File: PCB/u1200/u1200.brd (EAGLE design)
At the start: 243.8 x 243.8 mm, 120 parts, among them IC1 74LS74D, J1 ATX24RH, P1 CBM_A1200_EDGE_CONNECTOR, U16 DRAM_256KX16, U17 DRAM_256KX16, U18 DRAM_256KX16, U19 DRAM_256KX16, U2 CBM_8374, U20 CBM_391425, U4 CBM_4203, U6A AM29F400S, U6B AM29F400S

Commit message: A and DRA bus manual routing
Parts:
- removed R151A, R151B, R151C, R151D, R151E, R151F, R151G, R151H: 68, rcl:R0805
- added R151AH: 742C043680JP, Resistor Array:742C163220JP
- R151I: device rcl:R0805 -> rcl:R0603
- moved ROM_SW 192.8 mm to (226.1, 118.1)
- moved U20 175.8 mm to (205.7, 0.00)
- moved E131C 91.5 mm to (139.7, 63.5)
- moved E131R 91.5 mm to (139.7, 61.0)
- moved R100 91.5 mm to (139.7, 58.4)
- moved R592 82.4 mm to (131.8, 9.91)
- moved R953A 82.4 mm to (131.8, 5.33)
- moved R953B 82.4 mm to (131.8, 7.62)
- moved R953C 82.4 mm to (131.8, 30.5)
- moved R953D 82.4 mm to (131.8, 28.2)
- moved R953E 82.4 mm to (131.8, 25.9)
- moved R953F 82.4 mm to (131.8, 23.6)
- moved R954A 82.4 mm to (131.8, 21.3)
- moved R954B 82.4 mm to (131.8, 19.1)
- moved R954C 82.4 mm to (131.8, 16.8)
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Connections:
- net A17: now also U6A.3; no longer U6A.34
- net A18: now also U6A.34
- net A19: no longer U6A.3
- net BDRA0: now also R151AH.16; no longer R151A.2
- net BDRA1: now also R151AH.15; no longer R151B.2
- net BDRA2: now also R151AH.14; no longer R151C.2
- net BDRA3: now also R151AH.13; no longer R151D.2
- net BDRA4: now also R151AH.12; no longer R151E.2
- net BDRA5: now also R151AH.11; no longer R151F.2
- net BDRA6: now also R151AH.10; no longer R151G.2
- net BDRA7: now also R151AH.9; no longer R151H.2
- net DRA0: now also R151AH.1; no longer R151A.1
- net DRA1: now also R151AH.2; no longer R151B.1
- net DRA2: now also R151AH.3; no longer R151C.1
- net DRA3: now also R151AH.4; no longer R151D.1
- net DRA4: now also R151AH.5; no longer R151E.1
- net DRA5: now also R151AH.6; no longer R151F.1
- net DRA6: now also R151AH.7; no longer R151G.1
- net DRA7: now also R151AH.8; no longer R151H.1
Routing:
- net A10: track 0.00 -> 139.1 mm
- net A19: track 0.00 -> 87.5 mm
- net DRD0: track 0.00 -> 73.1 mm
- net A11: track 0.00 -> 61.3 mm
- net A8: track 0.00 -> 61.2 mm
- net A9: track 0.00 -> 61.1 mm
- net _BRAS_UU: track 0.00 -> 60.3 mm, vias 0 -> 1
- net _BRAS_UM: track 0.00 -> 59.9 mm, vias 0 -> 1
- net DRD18: track 0.00 -> 52.7 mm, vias 0 -> 1
- net DRD17: track 0.00 -> 52.6 mm, vias 0 -> 1
- net DRD16: track 0.00 -> 52.2 mm, vias 0 -> 1
- net A7: track 0.00 -> 47.4 mm
- net A12: track 0.00 -> 46.8 mm
- net A13: track 0.00 -> 45.9 mm
- net A15: track 0.00 -> 44.9 mm
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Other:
- board text removed: "CBM 391425 "BUDGIE""
- board text removed: "CBM 8374 "ALICE""
- board text removed: "Kickstart - High Word"
- board text removed: "Kickstart - Low Word"
- board text removed: "U2"
- board text removed: "U20"

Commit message: a0-a20 bus from edge connector to chip ram
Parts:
- moved X1 229.3 mm to (231.1, 132.1)
- moved U20 177.9 mm to (67.3, 111.8)
- moved U6B 33.0 mm to (57.1, 77.5), turned to 0 degrees
- moved U6A 16.3 mm to (57.1, 55.9), turned to 0 degrees
- moved C902 11.5 mm to (9.65, 25.4)
- moved C901 10.2 mm to (10.2, 27.9)
- moved R593 8.77 mm to (28.3, 26.0), turned to 180 degrees
- moved IC1 7.62 mm to (20.3, 29.2), turned to 0 degrees
- moved R902 6.35 mm to (5.46, 30.5)
- moved R901 5.08 mm to (5.46, 27.9)
- moved R903 3.81 mm to (5.46, 25.4)
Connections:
- net A17: no longer U6A.3
- net A19: now also U6A.3
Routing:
- net A20: track 0.00 -> 166.0 mm, vias 0 -> 2
- net A1: track 0.00 -> 135.6 mm
- net A0: track 0.00 -> 95.6 mm
- net A18: track 44.2 -> 129.4 mm, vias 0 -> 2
- net A17: track 41.2 -> 124.3 mm, vias 0 -> 1
- net A16: track 44.3 -> 122.0 mm, vias 0 -> 2
- net A15: track 44.9 -> 117.1 mm, vias 0 -> 1
- net A14: track 44.8 -> 116.7 mm, vias 0 -> 2
- net A13: track 45.9 -> 116.4 mm, vias 0 -> 1
- net A12: track 46.8 -> 111.5 mm, vias 0 -> 2
- net A5: track 44.5 -> 103.3 mm, vias 0 -> 1
- net A4: track 44.6 -> 102.2 mm
- net A2: track 41.9 -> 99.2 mm
- net A6: track 44.5 -> 101.8 mm
- net A3: track 43.1 -> 98.7 mm, vias 0 -> 1
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
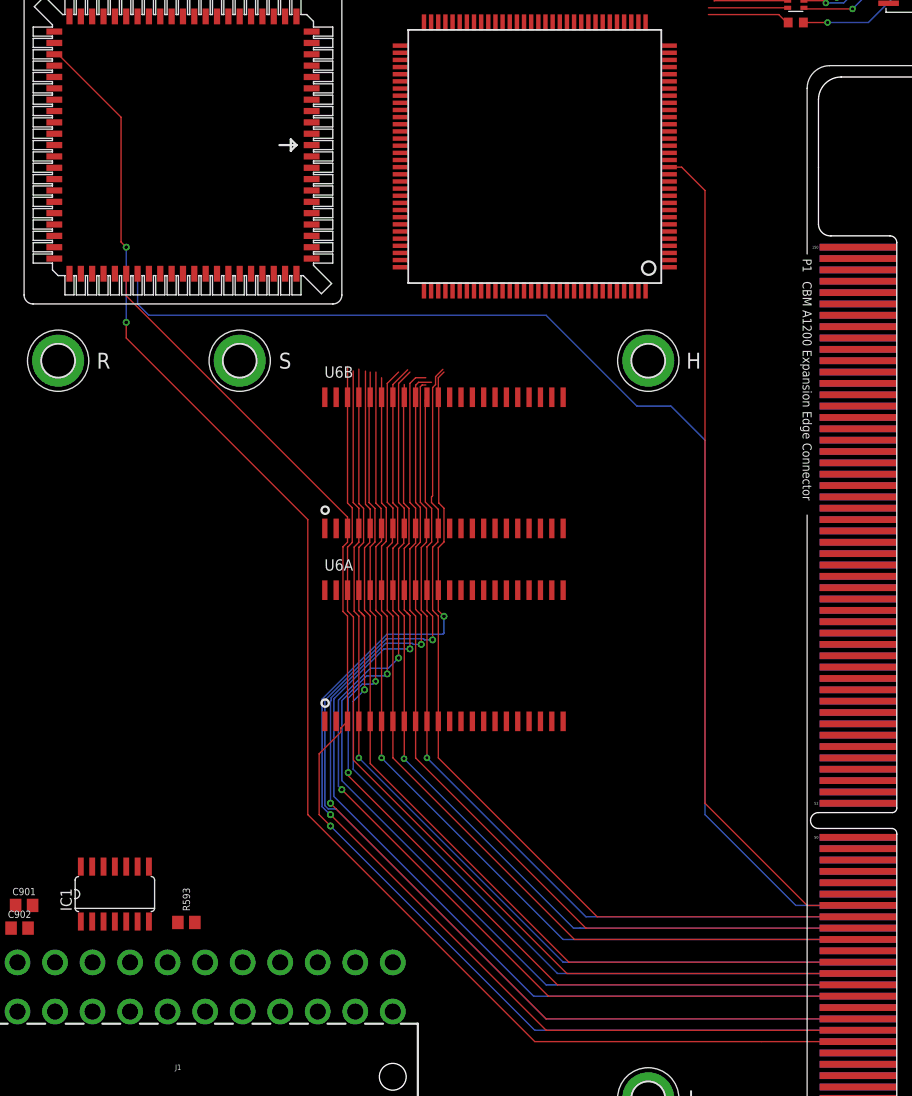
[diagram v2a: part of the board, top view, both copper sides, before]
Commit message: a0-a120 chipram/edge connector bus moved to top layer
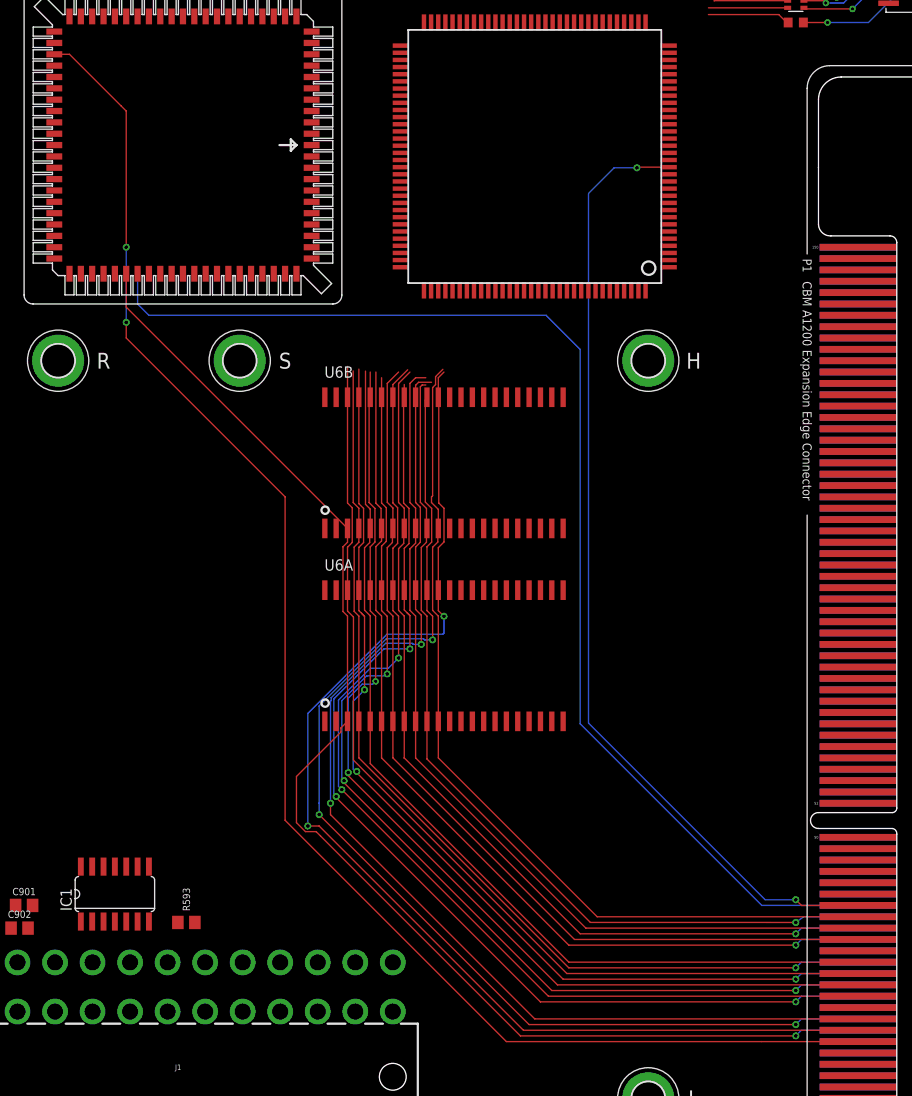
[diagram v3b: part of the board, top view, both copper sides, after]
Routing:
- net A0: track 95.6 -> 108.1 mm, vias 0 -> 2
- net A19: track 139.7 -> 147.5 mm
- net A11: track 109.2 -> 113.0 mm, vias 1 -> 3
- net A15: track 117.1 -> 120.9 mm, vias 1 -> 3
- net A9: track 106.2 -> 109.9 mm
- net A7: track 102.6 -> 106.3 mm
- net A18: track 129.4 -> 132.9 mm
- net A20: track 166.0 -> 168.6 mm
- net A17: track 124.3 -> 126.4 mm, vias 1 -> 3
- net A16: track 122.0 -> 122.7 mm
- net A13: track 116.4 -> 117.0 mm, vias 1 -> 3
- net A3: track 98.7 -> 99.2 mm

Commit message: Added License
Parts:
- removed R951A, R951B, R951C, R951D, R951E, R951F, R951G: 4.7K, rcl:R0805
- added R951AG: 741X163220JP, Resistor Array:741X163220JP
- R593: device rcl:R0805 -> rcl:R0603
- moved R593 72.9 mm to (76.2, 81.0)
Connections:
- net GND: no longer P1.P$141, P1.P$142, P1.P$145
- net R_W: now also R951AG.5; no longer R951E.1
- net SIZE_0: now also R951AG.3; no longer R951C.1
- net SIZE_1: now also R951AG.4; no longer R951D.1
- net VCC: now also R951AG.10, R951AG.11, R951AG.12, R951AG.13, R951AG.14, R951AG.15, R951AG.16; no longer R951A.2, R951B.2, R951C.2, R951D.2, R951E.2, R951F.2, R951G.2
- net _AS: now also R951AG.6; no longer R951F.1
- net _DS: now also R951AG.7; no longer R951G.1
- net _HLT: now also R951AG.1; no longer R951A.1
- net _RST: now also R951AG.2; no longer R951B.1
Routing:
- net _ROMEN: track 0.00 -> 49.6 mm, vias 0 -> 2
- net _WIDE: track 0.00 -> 26.4 mm
- net GND: track 0.00 -> 5.72 mm
- net A20: track 168.6 -> 165.7 mm
- net A18: track 132.9 -> 129.9 mm
- net A17: track 126.4 -> 124.1 mm
- net A16: track 122.7 -> 120.5 mm
- net A8: track 108.5 -> 106.6 mm
- net A13: track 117.0 -> 115.4 mm
- net A11: track 113.0 -> 111.5 mm
- net A10: track 111.2 -> 109.6 mm
- net A15: track 120.9 -> 119.4 mm
- net A12: track 111.5 -> 110.0 mm
- net A9: track 109.9 -> 108.4 mm
- net A6: track 101.8 -> 100.3 mm
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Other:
- board text added: "1D4:0.8"
- board text added: "CC BY-SA 4.0"
- board text added: "github.com/betajaen/u1200"
- board text removed: "1D4:0.7"

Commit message: Changed ROMs more traditional format. Re-routed A bus
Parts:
- removed R101, R103, R952A, R952B, R953A, R953B, R953C: 470, rcl:R0805
- removed ROM_SW: SWS002, smd-special:SMS-002
- added R101_104_952AB: 741X163220JP, Resistor Array:741X163220JP
- U6A, U6B: value AM29F400S -> CBM_A1200_ROM_U6AB; device am29-memory:SO44 -> u1200:CBM_A1200_ROM_DIL42
- moved E124C 41.6 mm to (80.3, 143.5)
- moved E124R 34.1 mm to (71.1, 140.3)
- moved R593 27.9 mm to (48.3, 81.7), turned to 270 degrees
- moved U6B 12.1 mm to (48.3, 69.2)
- moved C902 12.1 mm to (10.3, 37.5)
- moved R903 12.1 mm to (6.10, 37.5)
- moved C901 12.1 mm to (10.8, 40.0)
- moved R901 12.1 mm to (6.10, 40.0)
- moved R902 12.1 mm to (6.10, 42.5)
- moved R951AG 11.9 mm to (88.9, 65.4), turned to 180 degrees
- moved U6A 11.7 mm to (48.3, 48.3)
- moved IC1 8.47 mm to (12.1, 31.1)
- moved J1 1.42 mm to (27.1, 10.7)
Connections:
- removed net KS_FASTMODE: ROM_SW.1
- removed net WE_: ROM_SW.2, U6A.43, U6B.43
- net A10: now also U6A.41, U6B.41; no longer U6A.42, U6B.42
- net A11: now also U6A.40, U6B.40; no longer U6A.41, U6B.41
- net A12: now also U6A.39, U6B.39; no longer U6A.40, U6B.40
- net A13: now also U6A.38, U6B.38; no longer U6A.39, U6B.39
- net A14: now also U6A.37, U6B.37; no longer U6A.38, U6B.38
- net A15: now also U6A.36, U6B.36; no longer U6A.37, U6B.37
- net A16: now also U6A.35, U6B.35; no longer U6A.36, U6B.36
- net A17: now also U6A.34, U6B.34; no longer U6A.35, U6B.35
- net A18: now also U6A.33, U6B.33; no longer U6A.34, U6B.34
- net A19: no longer U6A.3, U6B.3
- net A2: now also U6A.10, U6B.10; no longer U6A.11, U6B.11
- net A3: now also U6A.9, U6B.9; no longer U6A.10, U6B.10
- net A4: now also U6A.8, U6B.8; no longer U6A.9, U6B.9
- net A5: now also U6A.7, U6B.7; no longer U6A.8, U6B.8
- net A6: now also U6A.6, U6B.6; no longer U6A.7, U6B.7
- net A7: now also U6A.5, U6B.5; no longer U6A.6, U6B.6
- net A8: now also U6A.4, U6B.4; no longer U6A.5, U6B.5
- net A9: now also U6A.3, U6B.3; no longer U6A.4, U6B.4
- net D0: now also U6B.14; no longer U6B.15
- net D1: now also U6B.16; no longer U6B.17
- net D10: now also U6B.19; no longer U6B.20
- net D11: now also U6B.21; no longer U6B.22
- net D12: now also U6B.24; no longer U6B.25
- net D13: now also U6B.26; no longer U6B.27
- net D14: now also U6B.28; no longer U6B.29
- net D15: now also U6B.30; no longer U6B.31
- net D16: now also U6A.14; no longer U6A.15
- net D17: now also U6A.16; no longer U6A.17
- net D18: now also U6A.18; no longer U6A.19
- net D19: now also U6A.20; no longer U6A.21
- net D2: now also U6B.18; no longer U6B.19
- net D20: now also U6A.23; no longer U6A.24
- net D21: now also U6A.25; no longer U6A.26
- net D22: now also U6A.27; no longer U6A.28
- net D23: now also U6A.29; no longer U6A.30
- net D24: now also U6A.15; no longer U6A.16
- net D25: now also U6A.17; no longer U6A.18
- net D26: now also U6A.19; no longer U6A.20
- net D27: now also U6A.21; no longer U6A.22
- net D28: now also U6A.24; no longer U6A.25
- net D29: now also U6A.26; no longer U6A.27
- net D3: now also U6B.20; no longer U6B.21
- net D30: now also U6A.28; no longer U6A.29
- net D31: now also U6A.30; no longer U6A.31
- net D4: now also U6B.23; no longer U6B.24
- net D5: now also U6B.25; no longer U6B.26
- net D6: now also U6B.27; no longer U6B.28
- net D7: now also U6B.29; no longer U6B.30
- net D8: now also U6B.15; no longer U6B.16
- net D9: now also U6B.17; no longer U6B.18
- net GND: now also U6A.12, U6A.31, U6B.12, U6B.31; no longer U6A.13, U6A.32, U6B.13, U6B.32
- net IPL0: now also R101_104_952AB.1; no longer R953A.1
- net IPL1: now also R101_104_952AB.2; no longer R953B.1
- net IPL2: now also R101_104_952AB.3; no longer R953C.1
- net R_W: now also R951AG.8; no longer R951AG.5
- net SIZE_0: now also R951AG.5; no longer R951AG.3
- net VCC: now also R101_104_952AB.10, R101_104_952AB.11, R101_104_952AB.12, R101_104_952AB.13, R101_104_952AB.14, R101_104_952AB.15, R101_104_952AB.16, R951AG.9, U6A.22, U6A.32, U6B.22, U6B.32; no longer R101.2, R103.2, R952A.2, R952B.2, R953A.2, R953B.2, R953C.2, ROM_SW.3, ROM_SW.4, U6A.23, U6A.33, U6B.23, U6B.33
- net _AVEC: now also R101_104_952AB.5; no longer R103.1
- net _BEER: now also R101_104_952AB.4; no longer R101.1
- net _DSACK_0: now also R101_104_952AB.6; no longer R952A.1
- net _DSACK_1: now also R101_104_952AB.7; no longer R952B.1
- net _HLT: now also R951AG.2; no longer R951AG.1
- net _OE: now also U6A.13, U6B.13; no longer U6A.14, U6B.14
- net _ROMEN: now also U6A.11, U6B.11; no longer U6A.12, U6B.12
- net _RST: now also R951AG.3; no longer R951AG.2
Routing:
- net A20: track 165.7 -> 0.00 mm, vias 2 -> 0
- net A19: track 146.9 -> 0.00 mm, vias 1 -> 0
- net A1: track 135.6 -> 0.00 mm
- net A0: track 108.1 -> 0.00 mm, vias 2 -> 0
- net BDRA8: track 68.5 -> 0.00 mm, vias 2 -> 0
- net _ROE: track 68.0 -> 0.00 mm, vias 2 -> 0
- net BDRA7: track 67.5 -> 0.00 mm, vias 2 -> 0
- net BDRA6: track 66.6 -> 0.00 mm, vias 2 -> 0
- net BDRA5: track 66.1 -> 0.00 mm, vias 2 -> 0
- net BDRA4: track 66.1 -> 0.00 mm
- net _BRAS_UU: track 60.3 -> 0.00 mm, vias 1 -> 0
- net _BRAS_UM: track 59.9 -> 0.00 mm, vias 1 -> 0
- net BDRA3: track 57.5 -> 0.00 mm
- net _BRAS(0): track 57.4 -> 0.00 mm
- net BDRA2: track 55.6 -> 0.00 mm
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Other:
- board text added: "E"
- board text added: "HIGH"
- board text added: "LOW"
- board text added: "P"
